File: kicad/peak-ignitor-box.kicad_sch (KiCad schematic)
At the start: 145 parts, among them J1 +24V, J10 SW, J11 Conn_01x01, J12 Conn_01x01, J13 Conn_01x01, J14 Conn_01x01, J15 GND, J2 GND, J3 PROG, J4 JTAG, J5 BATT, J6 GND, J7 +12V, J8 Barrel_Jack, J9 BATT-sw, Q1 BSS138, Q2 BSS138, Q3 IRLML9301, Q4 NVTFS5C454NLWFTAG, Q5 NVTFS5C454NLWFTAG, Q6 NVTFS5C454NLWFTAG, Q7 NVTFS5C454NLWFTAG, Q8 NVTFS5C454NLWFTAG, Q9 NVTFS5C454NLWFTAG, SW1 GT-TC029B-H025-L1N, SW2 GT-TC029B-H025-L1N, SW4 SW_Push, U1 TMP1075, U2 TMP1075, U3 ESP32-S3-MINI-1, U4 BQ24600, U5 AP3211, U6 LM51770DCPR, X1 20A-spare, X2 20A-spare, X3 20A-spare

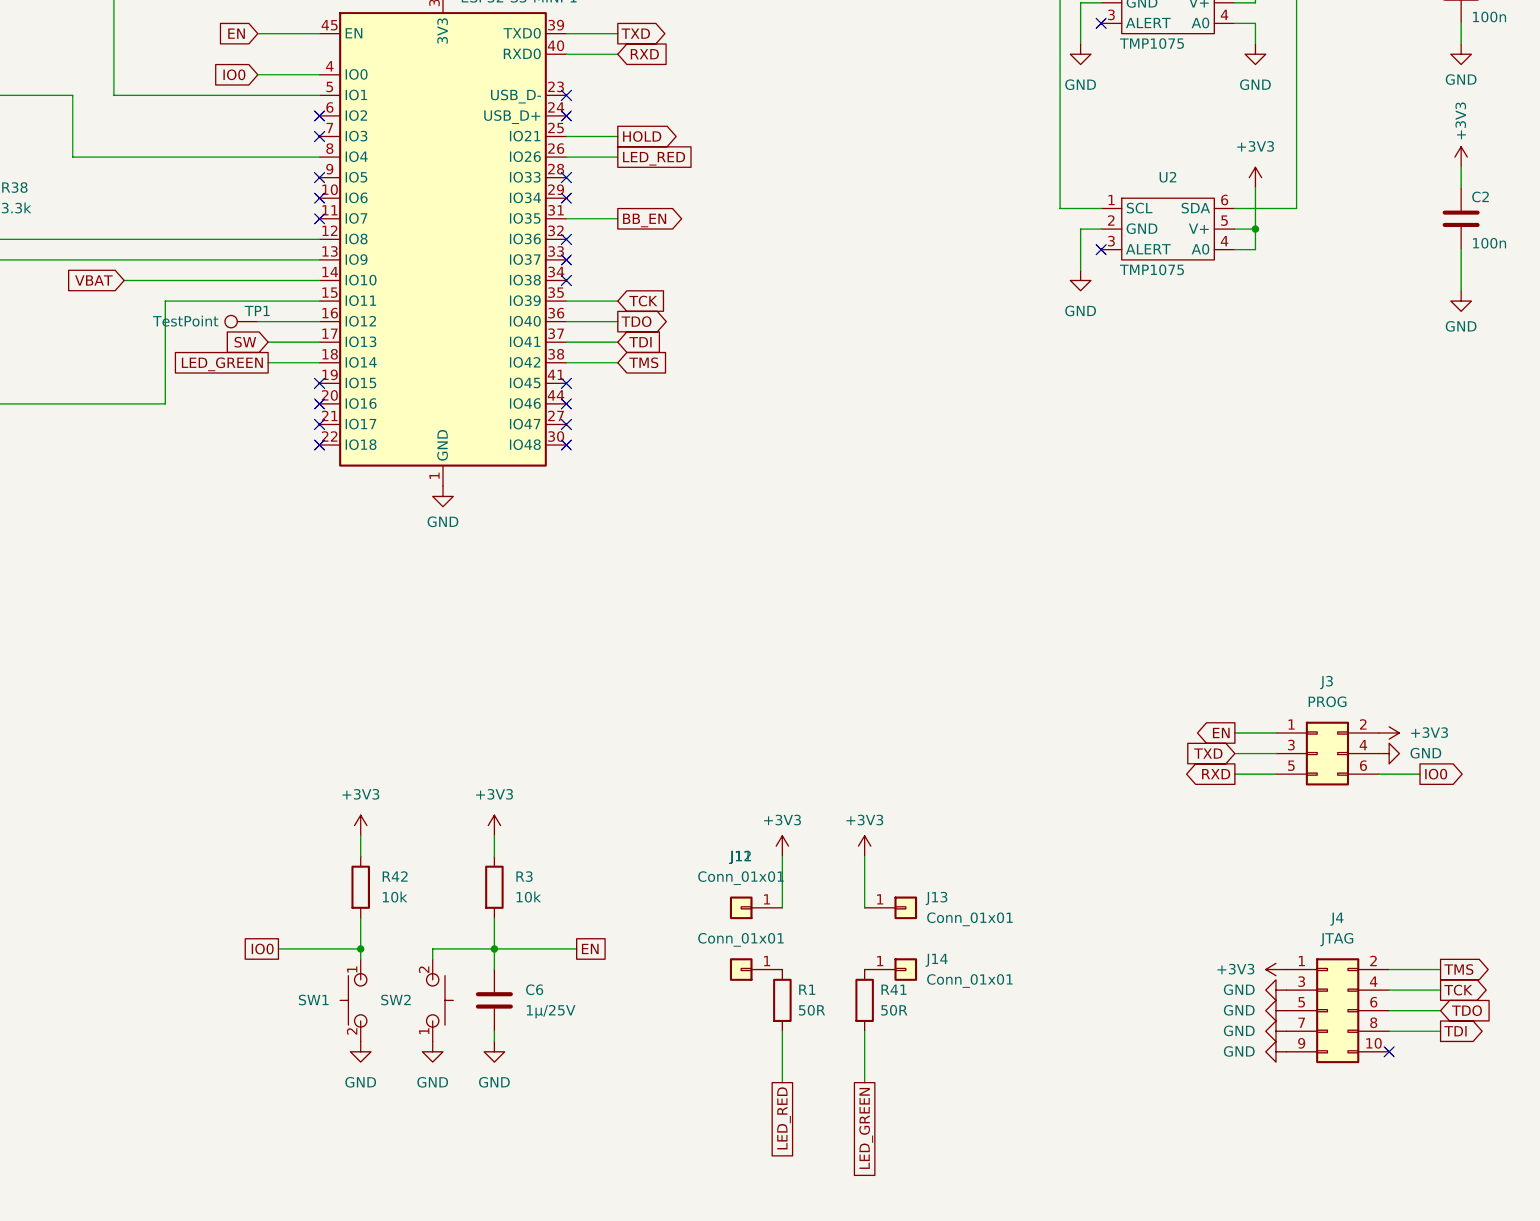
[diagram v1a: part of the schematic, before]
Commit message: added 160W discharge
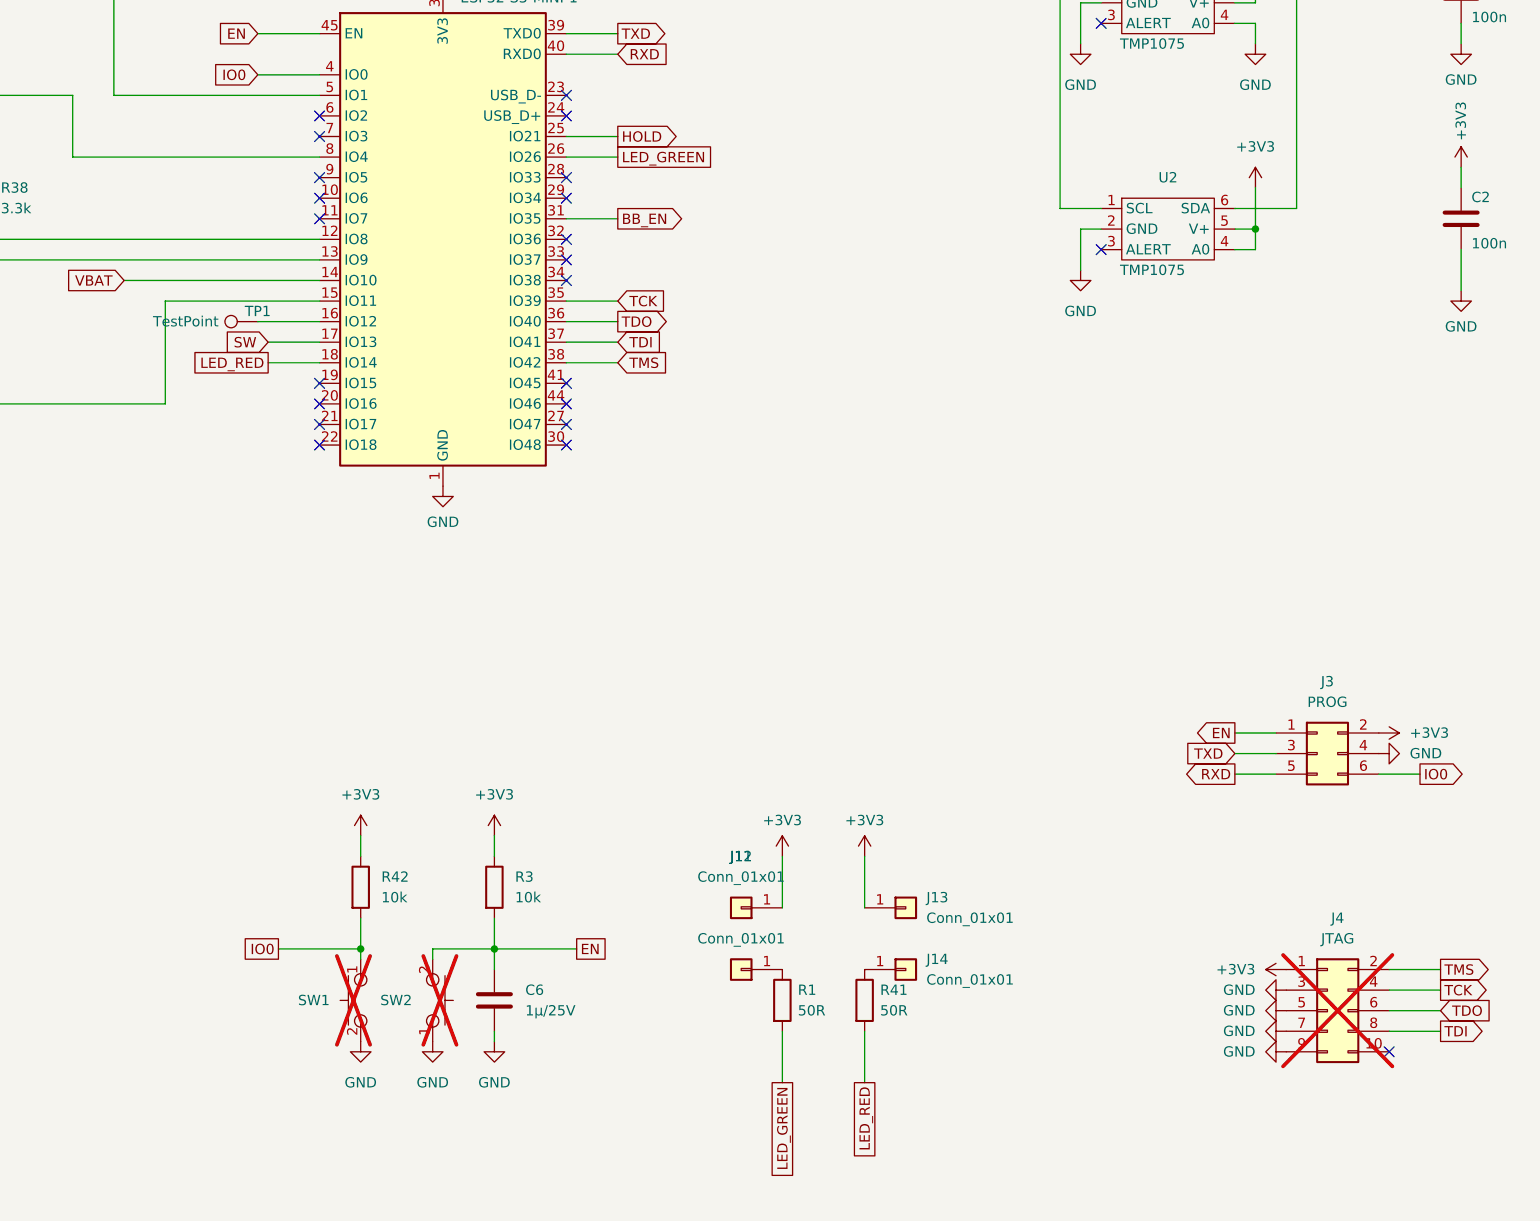
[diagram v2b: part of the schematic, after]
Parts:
- J4, SW1, SW2: now not fitted
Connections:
- net LED_GREEN: now also R1.2, U3.26 (IO26); no longer R41.2, U3.18 (IO14)
- net LED_RED: now also R41.2, U3.18 (IO14); no longer R1.2, U3.26 (IO26)
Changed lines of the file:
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@@
 		)
 	)
-	(global_label "LED_GREEN"
+	(global_label "LED_RED"
 		(shape passive)
 		(at 154.94 397.51 270)
@@
 		)
 		(property "Intersheetrefs" "${INTERSHEET_REFS}"
-			(at 154.94 409.4717 90)
+			(at 154.94 406.9922 90)
 			(effects
 				(font
@@
 		)
 	)
-	(global_label "LED_GREEN"
+	(global_label "LED_RED"
 		(shape passive)
 		(at 81.28 308.61 180)
@@
 		)
 		(property "Intersheetrefs" "${INTERSHEET_REFS}"
-			(at 69.3183 308.61 0)
+			(at 71.7978 308.61 0)
 			(effects
 				(font
@@
 		)
 	)
-	(global_label "LED_RED"
+	(global_label "LED_GREEN"
 		(shape passive)
 		(at 144.78 397.51 270)
@@
 		)
 		(property "Intersheetrefs" "${INTERSHEET_REFS}"
-			(at 144.78 406.9922 90)
+			(at 144.78 409.4717 90)
 			(effects
 				(font
@@
 		)
 	)
-	(global_label "LED_RED"
+	(global_label "LED_GREEN"
 		(shape passive)
 		(at 124.46 283.21 0)
@@
 		)
 		(property "Intersheetrefs" "${INTERSHEET_REFS}"
-			(at 133.9422 283.21 0)
+			(at 136.4217 283.21 0)
 			(effects
 				(font
@@
 		(in_bom yes)
 		(on_board yes)
-		(dnp no)
+		(dnp yes)
 		(property "Reference" "SW1"
 			(at 88.9 387.3499 90)
@@
 		(in_bom yes)
 		(on_board yes)
-		(dnp no)
+		(dnp yes)
 		(property "Reference" "SW2"
 			(at 99.06 387.3499 90)
@@
 		(in_bom yes)
 		(on_board yes)
-		(dnp no)
+		(dnp yes)
 		(fields_autoplaced yes)
 		(property "Reference" "J4"

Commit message: rev1.1
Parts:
- added C46: 10µ/35V, Capacitor_SMD:C_1210_3225Metric, symbol Device:C
- added D6: SMCJ15A, Diode_SMD:D_SMC, symbol Diode:5KPxxA
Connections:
- net GND: now also C46.2, D6.2 (A2)
- net at C40.1, C41.1, C42.1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: no longer NT5.2, R33.1
- net at F3.1, NT4.2, R35.2: now also NT5.2, R33.1, C46.1
- net at F3.2, J7.1 (Pin_1): now also D6.1 (A1)
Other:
- moved on the sheet: C1, C10, C11, C12, C13, C14, C15, C16, C17, C18, C19, C2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

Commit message: push
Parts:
- removed NT5: NetTie_2, NetTie:NetTie-2_SMD_Pad0.5mm, symbol Device:NetTie_2
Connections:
- net at C46.1, F3.1, NT4.2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: now also U6.20 (VOUT)
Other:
- note added: "FIXME: high impedance output. An additional OP should be used."
- moved on the sheet: R20
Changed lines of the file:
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@@
 		)
 	)
+	(text "FIXME: high impedance output. \nAn additional OP should be used."
+		(exclude_from_sim no)
+		(at 233.68 264.16 90)
+		(effects
+			(font
+				(size 1.27 1.27)
+			)
+		)
+	)
 	(text "misc"
 		(exclude_from_sim no)
@@
 	)
 	(junction
-		(at 239.395 218.44)
+		(at 238.125 218.44)
 		(diameter 0)
 		(color 0 0 0 0)
@@
 	(wire
 		(pts
-			(xy 239.395 267.97) (xy 239.395 283.21)
+			(xy 238.125 267.97) (xy 238.125 283.21)
 		)
 		(stroke
@@
 	(wire
 		(pts
-			(xy 297.815 218.44) (xy 239.395 218.44)
+			(xy 297.815 218.44) (xy 238.125 218.44)
 		)
 		(stroke
@@
 	(wire
 		(pts
-			(xy 239.395 218.44) (xy 239.395 260.35)
+			(xy 238.125 218.44) (xy 238.125 260.35)
 		)
 		(stroke
@@
 	(wire
 		(pts
-			(xy 537.845 115.57) (xy 537.845 170.18)
-		)
-		(stroke
-			(width 0)
-			(type default)
-		)
-	)
-	(wire
-		(pts
 			(xy 403.225 127) (xy 404.495 127)
 		)
@@
 	(wire
 		(pts
-			(xy 537.845 106.68) (xy 537.845 110.49)
+			(xy 537.845 106.68) (xy 537.845 170.18)
 		)
 		(stroke
@@
 	(wire
 		(pts
-			(xy 235.585 218.44) (xy 239.395 218.44)
+			(xy 234.315 218.44) (xy 238.125 218.44)
 		)
 		(stroke
@@
 	(global_label "BB_IMON"
 		(shape output)
-		(at 235.585 218.44 180)
+		(at 234.315 218.44 180)
 		(fields_autoplaced yes)
 		(effects
@@
 		)
 		(property "Intersheetrefs" "${INTERSHEET_REFS}"
-			(at 225.0292 218.44 0)
+			(at 223.7592 218.44 0)
 			(effects
 				(font
@@
 	(symbol
 		(lib_id "Device:R")
-		(at 239.395 264.16 0)
+		(at 238.125 264.16 0)
+		(mirror y)
 		(unit 1)
 		(exclude_from_sim no)
@@
 		(dnp no)
 		(property "Reference" "R20"
-			(at 231.775 262.89 0)
+			(at 245.745 262.89 0)
 			(effects
 				(font
@@
 		)
 		(property "Value" "88.7k"
-			(at 231.775 265.43 0)
+			(at 245.745 265.43 0)
 			(effects
 				(font
@@
 		)
 		(property "Footprint" "Resistor_SMD:R_0805_2012Metric"
-			(at 237.617 264.16 90)
+			(at 239.903 264.16 90)
 			(effects
 				(font
@@
 		)
 		(property "Datasheet" "~"
-			(at 239.395 264.16 0)
+			(at 238.125 264.16 0)
 			(effects
 				(font
@@
 		)
 		(property "Description" "Resistor"
-			(at 239.395 264.16 0)
+			(at 238.125 264.16 0)
 			(effects
 				(font
@@
 	(symbol
 		(lib_id "power:GND")
-		(at 239.395 283.21 0)
+		(at 238.125 283.21 0)
 		(unit 1)
 		(exclude_from_sim no)
@@
 		(fields_autoplaced yes)
 		(property "Reference" "#PWR059"
-			(at 239.395 289.56 0)
+			(at 238.125 289.56 0)
 			(effects
 				(font
@@
 		)
 		(property "Value" "GND"
-			(at 239.395 288.29 0)
+			(at 238.125 288.29 0)
 			(effects
 				(font
@@
 		)
 		(property "Footprint" ""
-			(at 239.395 283.21 0)
+			(at 238.125 283.21 0)
 			(effects
 				(font
@@
 		)
 		(property "Datasheet" ""
-			(at 239.395 283.21 0)
+			(at 238.125 283.21 0)
 			(effects
 				(font
@@
 		)
 		(property "Description" "Power symbol creates a global label with name \"GND\" , ground"
-			(at 239.395 283.21 0)
+			(at 238.125 283.21 0)
 			(effects
 				(font
@@
 					(unit 1)
 				)
-			)
-		)
-	)
-	(symbol
-		(lib_id "Device:NetTie_2")
-		(at 537.845 113.03 270)
-		(mirror x)
-		(unit 1)
-		(exclude_from_sim no)
-		(in_bom no)
-		(on_board yes)
-		(dnp no)
-		(property "Reference" "NT5"
-			(at 536.575 111.7599 90)
-			(effects
-				(font
-					(size 1.27 1.27)
-				)
-				(justify right)
-			)
-		)
-		(property "Value" "NetTie_2"
-			(at 536.575 114.2999 90)
-			(effects
-				(font
-					(size 1.27 1.27)
-				)
-				(justify right)
-			)
-		)
-		(property "Footprint" "NetTie:NetTie-2_SMD_Pad0.5mm"
-			(at 537.845 113.03 0)
-			(effects
-				(font
-					(size 1.27 1.27)
-				)
-				(hide yes)
-			)
-		)
-		(property "Datasheet" "~"
-			(at 537.845 113.03 0)
-			(effects
-				(font
-					(size 1.27 1.27)
-				)
-				(hide yes)
-			)
-		)
-		(property "Description" "Net tie, 2 pins"
-			(at 537.845 113.03 0)
-			(effects
-				(font
-					(size 1.27 1.27)
-				)
-				(hide yes)
-			)
-		)
-		(pin "2"
-		)
-		(pin "1"
-		)
-		(instances
-			(project "peak-ignitor-box"
-				(path "/f83baf2c-645b-4eaa-9e2e-814c12002028"
-					(reference "NT5")
-					(unit 1)
-				)
